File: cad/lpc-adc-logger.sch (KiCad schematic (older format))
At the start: 7 parts

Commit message: Updated schematic.
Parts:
- removed J?: Conn_01x04, symbol Conn_01x04
- removed J?: Audio-Jack-4, symbol Audio-Jack-4
- removed J?: Conn_Coaxial_Power, symbol Conn_Coaxial_Power
- added C1, C2: 10uF, symbol CP
- added J2: UART, symbol Conn_01x04_Male
- added J3: SWD, symbol Conn_01x04_Male
- added J4: ANALOG IN, symbol Screw_Terminal_01x08
- added R1, R2, R3, R4, R5, R6, R7, R8: 4.7K, symbol R
- added R10: 10K, symbol R
- added R9: 330, symbol R
- added SW1: SPS/SPM, symbol SW_DIP_x01
- added SW3: ERASE, symbol SW_DIP_x01
- J1: renamed from J?; value SD_Card -> SD CARD
- SW2: renamed from SW?; value SW_Push -> RESET
- U1: renamed from U?; value mbed_LPC1114FN28 -> LPC1114FN28
- gave numbers to parts that had none: 1
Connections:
- net labels added: GND, VCC
- wire segments 0 -> 77
- no-connect marks 0 -> 16
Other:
- note added: "0.1"
- note added: "2018/5/21"
- note added: "4ch Analog Data Logger"
- moved on the sheet: D1, J1, SW2, U1

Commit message: Added KiCAD files.
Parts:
- removed SW3: ERASE, symbol SW_DIP_x01
- added SW3: FLUSH, Buttons_Switches_THT:SW_Tactile_Straight_KSA0Axx1LFTR, symbol SW_Push
- added SW4: SD_DETECT, Buttons_Switches_THT:SW_DIP_x1_W7.62mm_Slide, symbol SW_DIP_x01
- C1, C2: footprint (none) -> Capacitors_THT:CP_Radial_D5.0mm_P2.50mm
- D1: footprint (none) -> LEDs:LED_D3.0mm
- J1: footprint 10067847-001 -> Connectors:SD_Card_Receptacle
- J2, J3: footprint (none) -> Pin_Headers:Pin_Header_Straight_1x04_Pitch2.54mm
- J4: footprint (none) -> Pin_Headers:Pin_Header_Straight_1x08_Pitch2.54mm
- R1, R10, R2, R3, R4, R5, R6, R7, R8, R9: footprint (none) -> Resistors_THT:R_Axial_DIN0204_L3.6mm_D1.6mm_P2.54mm_Vertical
- SW1: footprint (none) -> Buttons_Switches_THT:SW_DIP_x1_W7.62mm_Slide
- SW2: footprint (none) -> Buttons_Switches_THT:SW_Tactile_Straight_KSA0Axx1LFTR
- U1: footprint (none) -> Housings_DIP:DIP-28_W15.24mm_Socket_LongPads
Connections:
- net GND: now also SW3.2, SW4.1
- net at U1.14 (dp14): now also J1.10 (CARD_DETECT), SW4.2
- net at U1.17 (dp17): now also SW3.1
- no-connect marks 16 -> 14
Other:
- note removed: "0.1"
- note removed: "2018/5/21"
- note removed: "4ch Analog Data Logger"
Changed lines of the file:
@@
 EESchema Schematic File Version 2
+LIBS:lpc-adc-logger-cache
 LIBS:power
 LIBS:device
@@
 LIBS:mbed
 LIBS:switches
-LIBS:lpc-adc-logger-cache
 EELAYER 25 0
 EELAYER END
@@
 encoding utf-8
 Sheet 1 1
-Title ""
-Date ""
-Rev ""
-Comp ""
-Comment1 ""
-Comment2 ""
-Comment3 ""
-Comment4 ""
+Title "4ch Data Logger"
+Date "2018-05-01"
+Rev "v0.01"
+Comp "@tyamadajp / https://github.com/tai/lpc-adc-logger/"
+Comment1 "- Sends data to UART"
+Comment2 "- Saves data to pre-allocated LOG-0000.DAT on FAT/SD"
+Comment3 "- Takes up to 6.6V input (divided by half before ADC measurement)"
+Comment4 "4ch data logger with following features: "
 $EndDescr
 $Comp
@@
 F 0 "U1" H 6750 5050 60  0000 C CNN
 F 1 "LPC1114FN28" H 6750 3500 60  0000 C CNN
-F 2 "" H 7250 3600 60  0000 C CNN
+F 2 "Housings_DIP:DIP-28_W15.24mm_Socket_LongPads" H 7250 3600 60  0001 C CNN
 F 3 "" H 7250 3600 60  0000 C CNN
 	1    6750 4250
@@
 F 0 "J1" H 1600 4050 50  0000 C CNN
 F 1 "SD CARD" H 2850 2950 50  0000 C CNN
-F 2 "10067847-001" H 2450 3850 50  0001 C CNN
+F 2 "Connectors:SD_Card_Receptacle" H 2450 3850 50  0001 C CNN
 F 3 "" H 2250 3500 50  0001 C CNN
 	1    2250 3500
@@
 F 0 "SW2" H 9250 4400 50  0000 L CNN
 F 1 "RESET" H 9200 4240 50  0000 C CNN
-F 2 "" H 9200 4500 50  0001 C CNN
+F 2 "Buttons_Switches_THT:SW_Tactile_Straight_KSA0Axx1LFTR" H 9200 4500 50  0001 C CNN
 F 3 "" H 9200 4500 50  0001 C CNN
 	1    9200 4300
@@
 F 0 "D1" H 8600 3300 50  0000 C CNN
 F 1 "LED" H 8600 3100 50  0000 C CNN
-F 2 "" H 8600 3200 50  0001 C CNN
+F 2 "LEDs:LED_D3.0mm" H 8600 3200 50  0001 C CNN
 F 3 "" H 8600 3200 50  0001 C CNN
 	1    8600 3200
@@
 F 0 "R9" V 8680 2650 50  0000 C CNN
 F 1 "330" V 8600 2650 50  0000 C CNN
-F 2 "" V 8530 2650 50  0001 C CNN
+F 2 "Resistors_THT:R_Axial_DIN0204_L3.6mm_D1.6mm_P2.54mm_Vertical" V 8530 2650 50  0001 C CNN
 F 3 "" H 8600 2650 50  0001 C CNN
 	1    8600 2650
@@
 F 0 "R7" V 4530 5900 50  0000 C CNN
 F 1 "4.7K" V 4450 5900 50  0000 C CNN
-F 2 "" V 4380 5900 50  0001 C CNN
+F 2 "Resistors_THT:R_Axial_DIN0204_L3.6mm_D1.6mm_P2.54mm_Vertical" V 4380 5900 50  0001 C CNN
 F 3 "" H 4450 5900 50  0001 C CNN
 	1    4450 5900
@@
 F 0 "J2" H 2950 2100 50  0000 C CNN
 F 1 "UART" H 2950 1600 50  0000 C CNN
-F 2 "" H 2950 1900 50  0001 C CNN
+F 2 "Pin_Headers:Pin_Header_Straight_1x04_Pitch2.54mm" H 2950 1900 50  0001 C CNN
 F 3 "" H 2950 1900 50  0001 C CNN
 	1    2950 1900
@@
 F 0 "J3" H 2950 4800 50  0000 C CNN
 F 1 "SWD" H 2950 4300 50  0000 C CNN
-F 2 "" H 2950 4600 50  0001 C CNN
+F 2 "Pin_Headers:Pin_Header_Straight_1x04_Pitch2.54mm" H 2950 4600 50  0001 C CNN
 F 3 "" H 2950 4600 50  0001 C CNN
 	1    2950 4600
@@
 F 0 "R3" V 4230 5800 50  0000 C CNN
 F 1 "4.7K" V 4150 5800 50  0000 C CNN
-F 2 "" V 4080 5800 50  0001 C CNN
+F 2 "Resistors_THT:R_Axial_DIN0204_L3.6mm_D1.6mm_P2.54mm_Vertical" V 4080 5800 50  0001 C CNN
 F 3 "" H 4150 5800 50  0001 C CNN
 	1    4150 5800
@@
 F 0 "R2" V 4230 5500 50  0000 C CNN
 F 1 "4.7K" V 4150 5500 50  0000 C CNN
-F 2 "" V 4080 5500 50  0001 C CNN
+F 2 "Resistors_THT:R_Axial_DIN0204_L3.6mm_D1.6mm_P2.54mm_Vertical" V 4080 5500 50  0001 C CNN
 F 3 "" H 4150 5500 50  0001 C CNN
 	1    4150 5500
@@
 F 0 "R5" V 4530 5300 50  0000 C CNN
 F 1 "4.7K" V 4450 5300 50  0000 C CNN
-F 2 "" V 4380 5300 50  0001 C CNN
+F 2 "Resistors_THT:R_Axial_DIN0204_L3.6mm_D1.6mm_P2.54mm_Vertical" V 4380 5300 50  0001 C CNN
 F 3 "" H 4450 5300 50  0001 C CNN
 	1    4450 5300
@@
 F 0 "R8" V 4530 6200 50  0000 C CNN
 F 1 "4.7K" V 4450 6200 50  0000 C CNN
-F 2 "" V 4380 6200 50  0001 C CNN
+F 2 "Resistors_THT:R_Axial_DIN0204_L3.6mm_D1.6mm_P2.54mm_Vertical" V 4380 6200 50  0001 C CNN
 F 3 "" H 4450 6200 50  0001 C CNN
 	1    4450 6200
@@
 F 0 "R4" V 4230 6100 50  0000 C CNN
 F 1 "4.7K" V 4150 6100 50  0000 C CNN
-F 2 "" V 4080 6100 50  0001 C CNN
+F 2 "Resistors_THT:R_Axial_DIN0204_L3.6mm_D1.6mm_P2.54mm_Vertical" V 4080 6100 50  0001 C CNN
 F 3 "" H 4150 6100 50  0001 C CNN
 	1    4150 6100
@@
 F 0 "R6" V 4530 5600 50  0000 C CNN
 F 1 "4.7K" V 4450 5600 50  0000 C CNN
-F 2 "" V 4380 5600 50  0001 C CNN
+F 2 "Resistors_THT:R_Axial_DIN0204_L3.6mm_D1.6mm_P2.54mm_Vertical" V 4380 5600 50  0001 C CNN
 F 3 "" H 4450 5600 50  0001 C CNN
 	1    4450 5600
@@
 F 0 "J4" H 2950 6000 50  0000 C CNN
 F 1 "ANALOG IN" H 2950 5100 50  0000 C CNN
-F 2 "" H 2950 5600 50  0001 C CNN
+F 2 "Pin_Headers:Pin_Header_Straight_1x08_Pitch2.54mm" H 2950 5600 50  0001 C CNN
 F 3 "" H 2950 5600 50  0001 C CNN
 	1    2950 5600
@@
 F 0 "SW1" H 9200 3950 50  0000 C CNN
 F 1 "SPS/SPM" H 9200 3650 50  0000 C CNN
-F 2 "" H 9200 3800 50  0001 C CNN
+F 2 "Buttons_Switches_THT:SW_DIP_x1_W7.62mm_Slide" H 9200 3800 50  0001 C CNN
 F 3 "" H 9200 3800 50  0001 C CNN
 	1    9200 3800
@@
 F 0 "R1" V 4230 5200 50  0000 C CNN
 F 1 "4.7K" V 4150 5200 50  0000 C CNN
-F 2 "" V 4080 5200 50  0001 C CNN
+F 2 "Resistors_THT:R_Axial_DIN0204_L3.6mm_D1.6mm_P2.54mm_Vertical" V 4080 5200 50  0001 C CNN
 F 3 "" H 4150 5200 50  0001 C CNN
 	1    4150 5200
@@
 F 0 "C1" H 5475 3300 50  0000 L CNN
 F 1 "10uF" H 5475 3100 50  0000 L CNN
-F 2 "" H 5488 3050 50  0001 C CNN
+F 2 "Capacitors_THT:CP_Radial_D5.0mm_P2.50mm" H 5488 3050 50  0001 C CNN
 F 3 "" H 5450 3200 50  0001 C CNN
 	1    5450 3200
@@
 F 0 "C2" H 7875 3300 50  0000 L CNN
 F 1 "10uF" H 7875 3100 50  0000 L CNN
-F 2 "" H 7888 3050 50  0001 C CNN
+F 2 "Capacitors_THT:CP_Radial_D5.0mm_P2.50mm" H 7888 3050 50  0001 C CNN
 F 3 "" H 7850 3200 50  0001 C CNN
 	1    7850 3200
@@
 F 0 "R10" V 8880 2650 50  0000 C CNN
 F 1 "10K" V 8800 2650 50  0000 C CNN
-F 2 "" V 8730 2650 50  0001 C CNN
+F 2 "Resistors_THT:R_Axial_DIN0204_L3.6mm_D1.6mm_P2.54mm_Vertical" V 8730 2650 50  0001 C CNN
 F 3 "" H 8800 2650 50  0001 C CNN
 	1    8800 2650
 	-1   0    0    1
-$EndComp
-$Comp
-L SW_DIP_x01 SW3
-U 1 1 5B03483C
-P 9200 4700
-F 0 "SW3" H 9200 4850 50  0000 C CNN
-F 1 "ERASE" H 9200 4550 50  0000 C CNN
-F 2 "" H 9200 4700 50  0001 C CNN
-F 3 "" H 9200 4700 50  0001 C CNN
-	1    9200 4700
-	1    0    0    -1
 $EndComp
 Wire Wire Line
@@
 Connection ~ 9500 4300
 Wire Wire Line
-	7550 4700 8900 4700
+	7550 4700 9000 4700
 Wire Wire Line
 	3150 3300 3350 3300
 Connection ~ 3350 3600
-Text Notes 7350 7500 0    60   ~ 0
-4ch Analog Data Logger
-Text Notes 10550 7650 0    60   ~ 0
-0.1
-Text Notes 8150 7650 0    60   ~ 0
-2018/5/21
 Connection ~ 3750 1800
 NoConn ~ 7550 3700
@@
 NoConn ~ 5900 4000
 NoConn ~ 5900 4800
-NoConn ~ 5900 4900
 Connection ~ 7700 3200
 NoConn ~ 3150 3100
@@
 NoConn ~ 1350 3400
 NoConn ~ 1350 3600
-NoConn ~ 1350 3700
+Connection ~ 9500 4700
+$Comp
+L PWR_FLAG #FLG09
+U 1 1 5B03782C
+P 2000 1750
+F 0 "#FLG09" H 2000 1825 50  0001 C CNN
+F 1 "PWR_FLAG" H 2000 1900 50  0000 C CNN
+F 2 "" H 2000 1750 50  0001 C CNN
+F 3 "" H 2000 1750 50  0001 C CNN
+	1    2000 1750
+	-1   0    0    1
+$EndComp
+$Comp
+L VCC #PWR010
+U 1 1 5B03797A
+P 2000 1600
+F 0 "#PWR010" H 2000 1450 50  0001 C CNN
+F 1 "VCC" H 2000 1750 50  0000 C CNN
+F 2 "" H 2000 1600 50  0001 C CNN
+F 3 "" H 2000 1600 50  0001 C CNN
+	1    2000 1600
+	1    0    0    -1
+$EndComp
+Wire Wire Line
+	2000 1600 2000 1750
+$Comp
+L PWR_FLAG #FLG011
+U 1 1 5B037A56
+P 2350 1600
+F 0 "#FLG011" H 2350 1675 50  0001 C CNN
+F 1 "PWR_FLAG" H 2350 1750 50  0000 C CNN
+F 2 "" H 2350 1600 50  0001 C CNN
+F 3 "" H 2350 1600 50  0001 C CNN
+	1    2350 1600
+	1    0    0    -1
+$EndComp
+$Comp
+L GND #PWR012
+U 1 1 5B037AA0
+P 2350 1750
+F 0 "#PWR012" H 2350 1500 50  0001 C CNN
+F 1 "GND" H 2350 1600 50  0000 C CNN
+F 2 "" H 2350 1750 50  0001 C CNN
+F 3 "" H 2350 1750 50  0001 C CNN
+	1    2350 1750
+	1    0    0    -1
+$EndComp
+Wire Wire Line
+	2350 1750 2350 1600
+$Comp
+L SW_Push SW3
+U 1 1 5B04BCB3
+P 9200 4700
+F 0 "SW3" H 9250 4800 50  0000 L CNN
+F 1 "FLUSH" H 9200 4640 50  0000 C CNN
+F 2 "Buttons_Switches_THT:SW_Tactile_Straight_KSA0Axx1LFTR" H 9200 4900 50  0001 C CNN
+F 3 "" H 9200 4900 50  0001 C CNN
+	1    9200 4700
+	1    0    0    -1
+$EndComp
+Wire Wire Line
+	9400 4700 9500 4700
+Wire Wire Line
+	5900 4900 3950 4900
+Wire Wire Line
+	3950 4900 3950 5100
+Wire Wire Line
+	3950 5100 1200 5100
+Wire Wire Line
+	1200 5100 1200 3700
+Wire Wire Line
+	1200 3700 1350 3700
+$Comp
+L SW_DIP_x01 SW4
+U 1 1 5B04C58B
+P 3650 4900
+F 0 "SW4" H 3650 5050 50  0000 C CNN
+F 1 "SD_DETECT" H 3650 4750 50  0000 C CNN
+F 2 "Buttons_Switches_THT:SW_DIP_x1_W7.62mm_Slide" H 3650 4900 50  0001 C CNN
+F 3 "" H 3650 4900 50  0001 C CNN
+	1    3650 4900
+	1    0    0    -1
+$EndComp
+Connection ~ 3950 4900
+Connection ~ 3350 4900
 $EndSCHEMATC

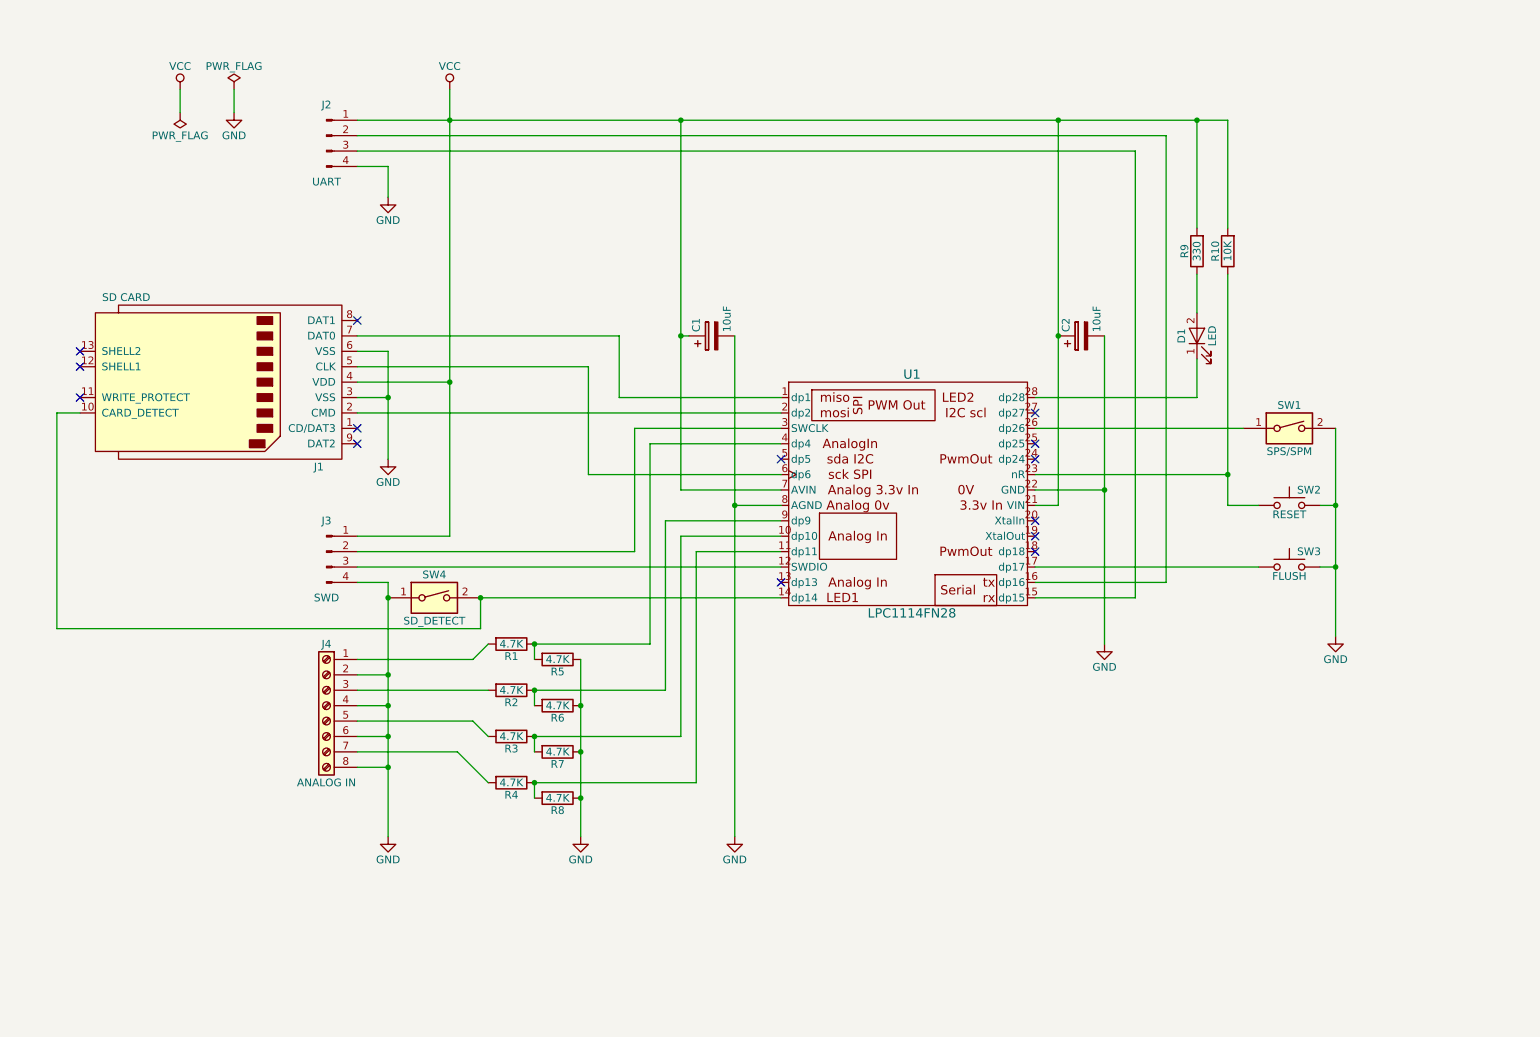
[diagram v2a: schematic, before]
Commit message: - Fixed SD card MMC-CS pin - Added GPIO header - Added I2C header
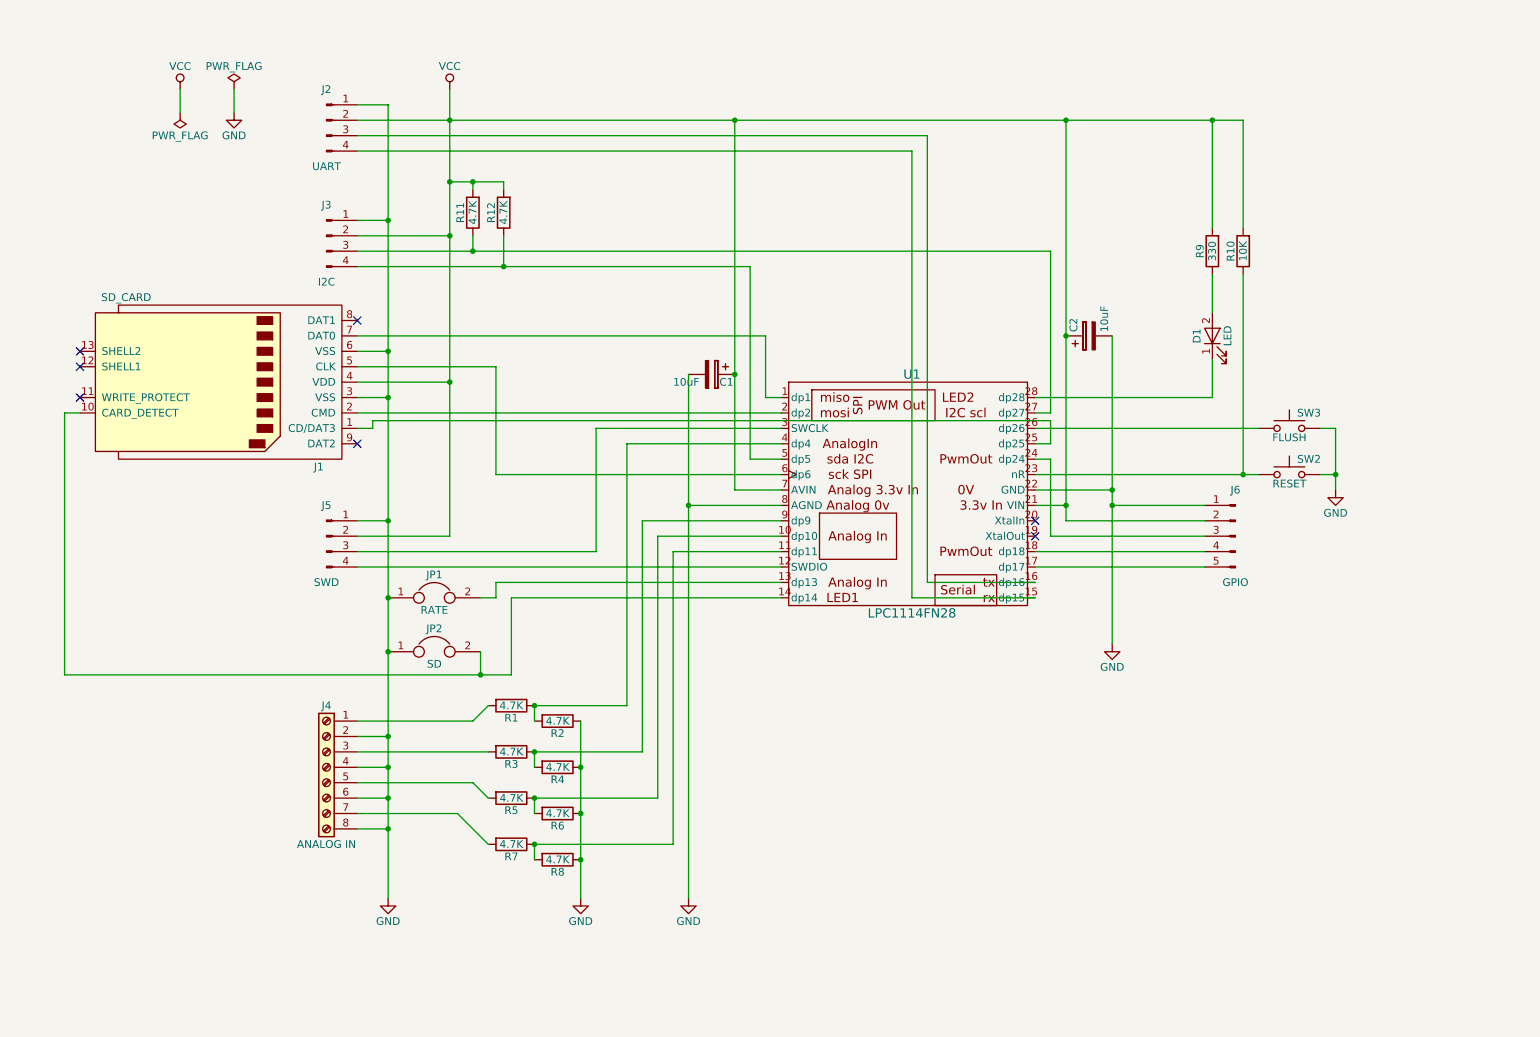
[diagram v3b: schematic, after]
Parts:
- removed SW1: SPS/SPM, Buttons_Switches_THT:SW_DIP_x1_W7.62mm_Slide, symbol SW_DIP_x01
- removed SW4: SD_DETECT, Buttons_Switches_THT:SW_DIP_x1_W7.62mm_Slide, symbol SW_DIP_x01
- added J5: SWD, Pin_Headers:Pin_Header_Straight_1x04_Pitch2.54mm, symbol Conn_01x04_Male
- added J6: GPIO, Pin_Headers:Pin_Header_Straight_1x05_Pitch2.54mm, symbol Conn_01x05_Male
- added JP1: RATE, Pin_Headers:Pin_Header_Straight_1x02_Pitch2.54mm, symbol Jumper
- added JP2: SD, Pin_Headers:Pin_Header_Straight_1x02_Pitch2.54mm, symbol Jumper
- added R11, R12: 4.7K, Resistors_THT:R_Axial_DIN0204_L3.6mm_D1.6mm_P2.54mm_Vertical, symbol R
- J1: value SD CARD -> SD_CARD
- J3: value SWD -> I2C
- renumbered R5 to R2, R2 to R3, R6 to R4, R3 to R5, R7 to R6, R4 to R7
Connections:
- net GND: now also J2.1 (Pin_1), J3.1 (Pin_1), J5.1 (Pin_1), J6.1 (Pin_1), JP1.1, JP2.1; no longer J2.4 (Pin_4), J3.4 (Pin_4)
- net VCC: now also J2.2 (Pin_2), J3.2 (Pin_2), J5.2 (Pin_2), J6.2 (Pin_2), R11.2, R12.2; no longer J2.1 (Pin_1), J3.1 (Pin_1)
- net at U1.12 (SWDIO): now also J5.4 (Pin_4); no longer J3.3 (Pin_3)
- net at U1.13 (dp13): now also JP1.2
- net at J1.10 (CARD_DETECT), U1.14 (dp14): now also JP2.2
- net at U1.15 (dp15): now also J2.4 (Pin_4); no longer J2.3 (Pin_3)
- net at U1.16 (dp16): now also J2.3 (Pin_3); no longer J2.2 (Pin_2)
- net at U1.17 (dp17): now also J6.5 (Pin_5); no longer SW3.1
- net at U1.18 (dp18): now also J6.4 (Pin_4)
- net at U1.24 (dp24): now also J6.3 (Pin_3)
- net at U1.25 (dp25): now also J1.1 (CD/DAT3)
- net at U1.26 (dp26): now also SW3.1
- net at U1.27 (dp27): now also J3.3 (Pin_3), R11.1
- net at U1.3 (SWCLK): now also J5.3 (Pin_3); no longer J3.2 (Pin_2)
- net at U1.5 (dp5): now also J3.4 (Pin_4), R12.1
- no-connect marks 14 -> 7
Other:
- moved on the sheet: C1, C2, D1, J4, R1, R10, R2, R3, R4, R5, R6, R7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

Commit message: [WIP] Added SPI header.
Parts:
- added J7: SPI, Pin_Headers:Pin_Header_Straight_1x06_Pitch2.54mm, symbol Conn_01x06_Male
- JP2: value SD -> CARD
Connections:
- net GND: now also J7.1 (Pin_1)
- net at J1.7 (DAT0), U1.1 (dp1): now also J7.3 (Pin_3)
- net at J1.2 (CMD), U1.2 (dp2): now also J7.4 (Pin_4)
- net at J1.1 (CD/DAT3), U1.25 (dp25): now also J7.6 (Pin_6)
- net at J1.5 (CLK), U1.6 (dp6): now also J7.2 (Pin_2), J7.5 (Pin_5)
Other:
- moved on the sheet: C1, C2, D1, J1, J2, J3, J4, J5, J6, JP1, JP2, R1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
